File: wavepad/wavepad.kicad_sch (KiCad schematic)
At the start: 18 parts, among them SW1 SW_Push, SW2 SW_Push, SW3 SW_Push, SW4 SW_Push, SW5 SW_Push, SW6 SW_Push, SW7 SW_Push, SW8 SW_Push, U1 Seeed Studio XIAO SAMD21

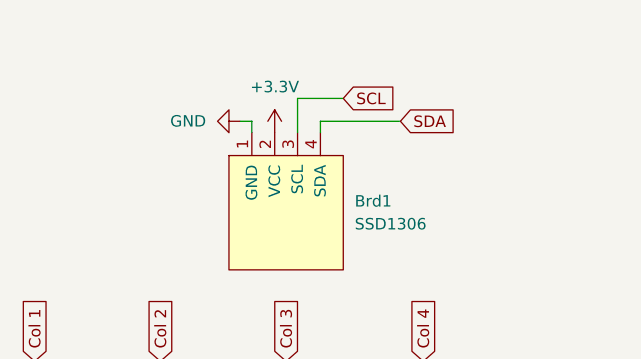
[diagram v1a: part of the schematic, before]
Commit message: add resistors to oled
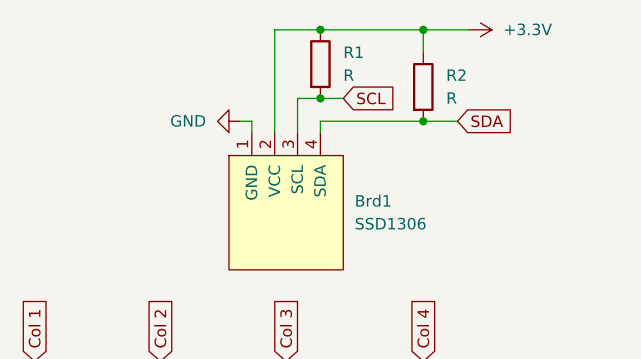
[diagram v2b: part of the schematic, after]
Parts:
- added R1, R2: R, Resistor_THT:R_Axial_DIN0309_L9.0mm_D3.2mm_P15.24mm_Horizontal, symbol Device:R
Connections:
- net +3.3V: now also R1.1, R2.1
- net SCL: now also R1.2
- net SDA: now also R2.2
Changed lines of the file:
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@@
 	(paper "A4")
+	(junction
+		(at 173.99 27.94)
+		(diameter 0)
+		(color 0 0 0 0)
+	)
+	(junction
+		(at 173.99 17.78)
+		(diameter 0)
+		(color 0 0 0 0)
+	)
 	(junction
 		(at 158.75 63.5)
@@
 	)
 	(junction
+		(at 162.56 17.78)
+		(diameter 0)
+		(color 0 0 0 0)
+	)
+	(junction
 		(at 170.18 97.79)
+		(diameter 0)
+		(color 0 0 0 0)
+	)
+	(junction
+		(at 162.56 25.4)
 		(diameter 0)
 		(color 0 0 0 0)
@@
 	(wire
 		(pts
-			(xy 162.56 27.94) (xy 171.45 27.94)
+			(xy 162.56 27.94) (xy 173.99 27.94)
 		)
 		(stroke
@@
 	(wire
 		(pts
+			(xy 157.48 17.78) (xy 157.48 29.21)
+		)
+		(stroke
+			(width 0)
+			(type default)
+		)
+	)
+	(wire
+		(pts
 			(xy 172.72 87.63) (xy 173.99 87.63)
 		)
@@
 	(wire
 		(pts
+			(xy 173.99 17.78) (xy 162.56 17.78)
+		)
+		(stroke
+			(width 0)
+			(type default)
+		)
+	)
+	(wire
+		(pts
 			(xy 144.78 87.63) (xy 146.05 87.63)
 		)
@@
 	(wire
 		(pts
+			(xy 162.56 25.4) (xy 165.1 25.4)
+		)
+		(stroke
+			(width 0)
+			(type default)
+		)
+	)
+	(wire
+		(pts
+			(xy 179.07 17.78) (xy 173.99 17.78)
+		)
+		(stroke
+			(width 0)
+			(type default)
+		)
+	)
+	(wire
+		(pts
 			(xy 130.81 63.5) (xy 130.81 87.63)
 		)
@@
 	(wire
 		(pts
+			(xy 173.99 27.94) (xy 177.8 27.94)
+		)
+		(stroke
+			(width 0)
+			(type default)
+		)
+	)
+	(wire
+		(pts
 			(xy 142.24 87.63) (xy 142.24 90.17)
 		)
@@
 	(wire
 		(pts
-			(xy 160.02 25.4) (xy 165.1 25.4)
+			(xy 160.02 25.4) (xy 162.56 25.4)
 		)
 		(stroke
@@
 	(wire
 		(pts
+			(xy 173.99 17.78) (xy 173.99 20.32)
+		)
+		(stroke
+			(width 0)
+			(type default)
+		)
+	)
+	(wire
+		(pts
 			(xy 160.02 29.21) (xy 160.02 25.4)
 		)
@@
 		(pts
 			(xy 173.99 87.63) (xy 175.26 87.63)
+		)
+		(stroke
+			(width 0)
+			(type default)
+		)
+	)
+	(wire
+		(pts
+			(xy 162.56 17.78) (xy 157.48 17.78)
 		)
 		(stroke
@@
 	(global_label "SDA"
 		(shape input)
-		(at 171.45 27.94 0)
+		(at 177.8 27.94 0)
 		(fields_autoplaced yes)
 		(effects
@@
 		)
 		(property "Intersheetrefs" "${INTERSHEET_REFS}"
-			(at 178.0033 27.94 0)
+			(at 184.3533 27.94 0)
 			(effects
 				(font
@@
 	)
 	(symbol
+		(lib_id "Device:R")
+		(at 162.56 21.59 0)
+		(unit 1)
+		(exclude_from_sim no)
+		(in_bom yes)
+		(on_board yes)
+		(dnp no)
+		(fields_autoplaced yes)
+		(property "Reference" "R1"
+			(at 165.1 20.3199 0)
+			(effects
+				(font
+					(size 1.27 1.27)
+				)
+				(justify left)
+			)
+		)
+		(property "Value" "R"
+			(at 165.1 22.8599 0)
+			(effects
+				(font
+					(size 1.27 1.27)
+				)
+				(justify left)
+			)
+		)
+		(property "Footprint" "Resistor_THT:R_Axial_DIN0309_L9.0mm_D3.2mm_P15.24mm_Horizontal"
+			(at 160.782 21.59 90)
+			(effects
+				(font
+					(size 1.27 1.27)
+				)
+				(hide yes)
+			)
+		)
+		(property "Datasheet" "~"
+			(at 162.56 21.59 0)
+			(effects
+				(font
+					(size 1.27 1.27)
+				)
+				(hide yes)
+			)
+		)
+		(property "Description" "Resistor"
+			(at 162.56 21.59 0)
+			(effects
+				(font
+					(size 1.27 1.27)
+				)
+				(hide yes)
+			)
+		)
+		(pin "2"
+		)
+		(pin "1"
+		)
+		(instances
+			(project "wavepad"
+				(path "/123ad757-6526-4e7e-bd36-20c32f5646db"
+					(reference "R1")
+					(unit 1)
+				)
+			)
+		)
+	)
+	(symbol
 		(lib_id "Diode:1N4148")
 		(at 156.21 93.98 90)
@@
 	(symbol
 		(lib_id "power:+3.3V")
-		(at 157.48 29.21 0)
+		(at 179.07 17.78 270)
 		(unit 1)
 		(exclude_from_sim no)
@@
 		(fields_autoplaced yes)
 		(property "Reference" "#PWR04"
-			(at 157.48 33.02 0)
+			(at 175.26 17.78 0)
 			(effects
 				(font
@@
 		)
 		(property "Value" "+3.3V"
-			(at 157.48 24.13 0)
-			(effects
-				(font
-					(size 1.27 1.27)
-				)
+			(at 182.88 17.7799 90)
+			(effects
+				(font
+					(size 1.27 1.27)
+				)
+				(justify left)
 			)
 		)
 		(property "Footprint" ""
-			(at 157.48 29.21 0)
+			(at 179.07 17.78 0)
 			(effects
 				(font
@@
 		)
 		(property "Datasheet" ""
-			(at 157.48 29.21 0)
+			(at 179.07 17.78 0)
 			(effects
 				(font
@@
 		)
 		(property "Description" "Power symbol creates a global label with name \"+3.3V\""
-			(at 157.48 29.21 0)
+			(at 179.07 17.78 0)
 			(effects
 				(font
@@
 					(unit 1)
 				)
+			)
+		)
+	)
+	(symbol
+		(lib_id "Device:R")
+		(at 173.99 24.13 0)
+		(unit 1)
+		(exclude_from_sim no)
+		(in_bom yes)
+		(on_board yes)
+		(dnp no)
+		(fields_autoplaced yes)
+		(property "Reference" "R2"
+			(at 176.53 22.8599 0)
+			(effects
+				(font
+					(size 1.27 1.27)
+				)
+				(justify left)
+			)
+		)
+		(property "Value" "R"
+			(at 176.53 25.3999 0)
+			(effects
+				(font
+					(size 1.27 1.27)
+				)
+				(justify left)
+			)
+		)
+		(property "Footprint" "Resistor_THT:R_Axial_DIN0309_L9.0mm_D3.2mm_P15.24mm_Horizontal"
+			(at 172.212 24.13 90)
+			(effects
+				(font
+					(size 1.27 1.27)
+				)
+				(hide yes)
+			)
+		)
+		(property "Datasheet" "~"
+			(at 173.99 24.13 0)
+			(effects
+				(font
+					(size 1.27 1.27)
+				)
+				(hide yes)
+			)
+		)
+		(property "Description" "Resistor"
+			(at 173.99 24.13 0)
+			(effects
+				(font
+					(size 1.27 1.27)
+				)
+				(hide yes)
+			)
+		)
+		(pin "2"
+		)
+		(pin "1"
+		)
+		(instances
+			(project "wavepad"
+				(path "/123ad757-6526-4e7e-bd36-20c32f5646db"
+					(reference "R2")
+					(unit 1)
+				)
